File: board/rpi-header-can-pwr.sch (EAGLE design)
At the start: 60 parts, among them J1 U.FL, U1 MCP2515, U3 BME280, U4 RFM69HCW, U5 INA219BIDCNT, X1 RJ45-8L21-S, X2 RASPI_BOARD_B+#_E3

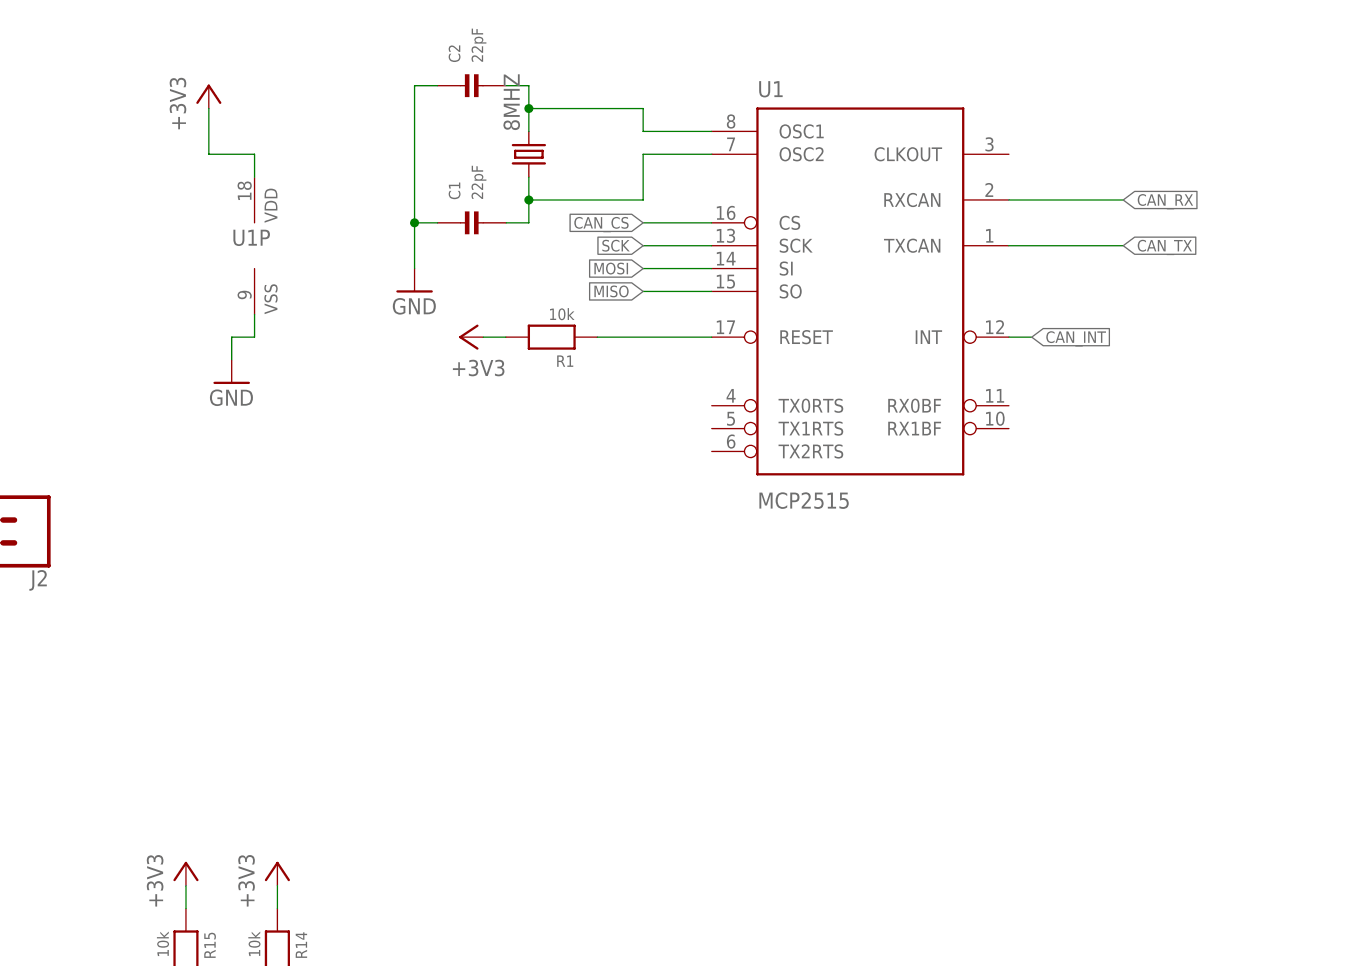
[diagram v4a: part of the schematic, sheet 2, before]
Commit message: MCP2515 increase pad size
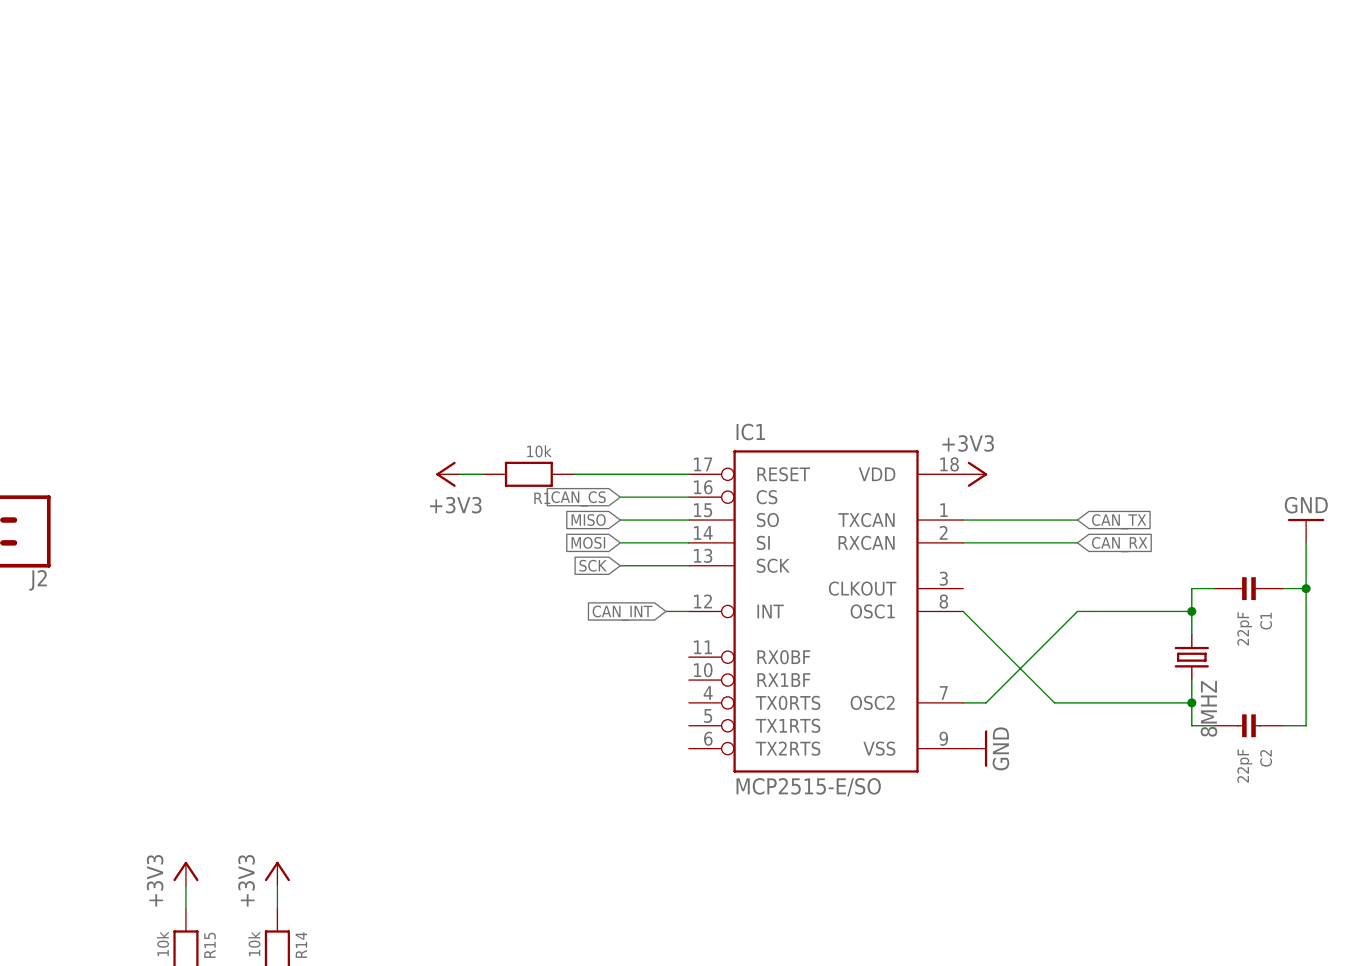
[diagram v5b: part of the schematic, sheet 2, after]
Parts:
- removed U1: MCP2515, SparkFun-DigitalIC:MCP2510SO
- added IC1: MCP2515-E/SO, mcp2515:MCP2515-E/SO
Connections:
- net +3V3: now also IC1.VDD; no longer U1P.VDD
- net CAN_CS: now also IC1.CS; no longer U1>NAME.CS
- net CAN_INT: now also IC1.INT; no longer U1>NAME.INT
- net CAN_RX: now also IC1.RXCAN; no longer U1>NAME.RXCAN
- net CAN_TX: now also IC1.TXCAN; no longer U1>NAME.TXCAN
- net GND: now also IC1.VSS; no longer U1P.VSS
- net MISO: now also IC1.SO; no longer U1>NAME.SO
- net MOSI: now also IC1.SI; no longer U1>NAME.SI
- net N$2: now also IC1.OSC1; no longer U1>NAME.OSC1
- net N$3: now also IC1.OSC2; no longer U1>NAME.OSC2
- net RS: now also IC1.RESET; no longer U1>NAME.RESET
- net SCK: now also IC1.SCK; no longer U1>NAME.SCK
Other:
- moved on the sheet: 8MHZ, C1, C2, R1

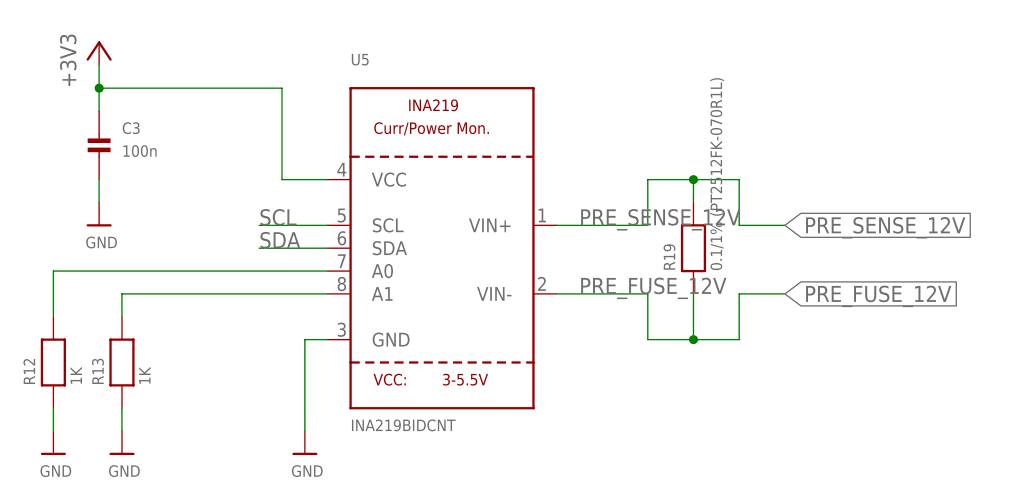
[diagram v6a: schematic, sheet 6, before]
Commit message: connect ina219 to i2c bus
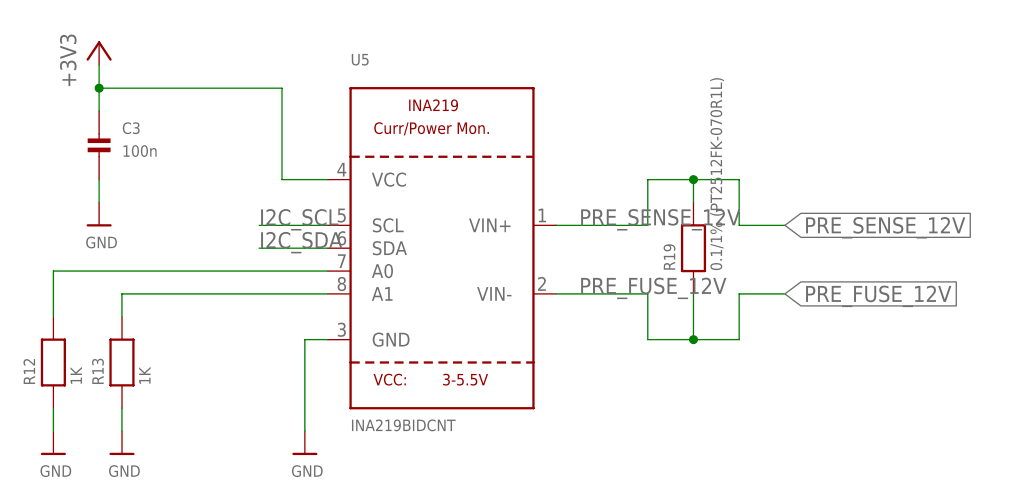
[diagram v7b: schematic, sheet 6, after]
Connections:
- removed net SCL: U5.SCL
- removed net SDA: U5.SDA
- net I2C_SCL: now also U5.SCL
- net I2C_SDA: now also U5.SDA
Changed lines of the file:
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@@
 </segment>
 </net>
-<net name="SDA" class="0">
+<net name="I2C_SDA" class="0">
 <segment>
 <wire x1="12.7" y1="53.34" x2="5.08" y2="53.34" width="0.1524" layer="91"/>
@@
 </segment>
 </net>
-<net name="SCL" class="0">
+<net name="I2C_SCL" class="0">
 <segment>
 <wire x1="12.7" y1="55.88" x2="5.08" y2="55.88" width="0.1524" layer="91"/>
